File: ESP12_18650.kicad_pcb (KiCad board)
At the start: 2 copper layers, 77.7 x 20.5 mm, 28 parts, among them J1 Conn_02x06_Counter_Clockwise, J10 Conn_01x06_Male, J11 Conn_01x06_Male, J12 Conn_01x06_Male, J13 Conn_01x06_Male, J14 Conn_01x06_Male, J15 Conn_01x06_Male, J16 Conn_01x06_Male, J17 Conn_01x14_Male, J2 Conn_01x14_Male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

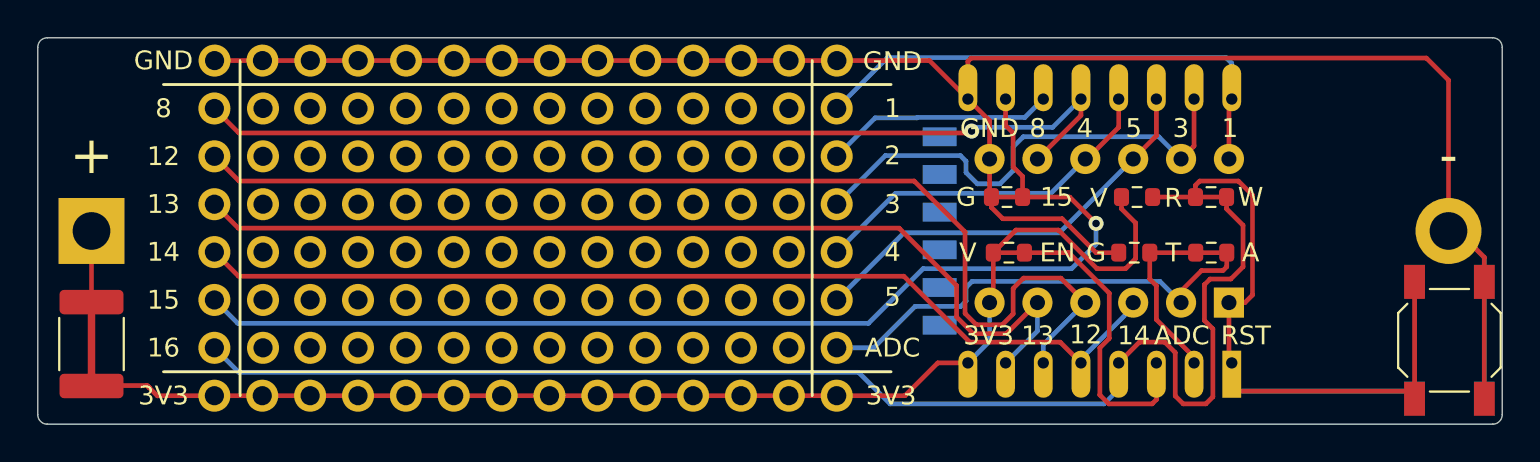
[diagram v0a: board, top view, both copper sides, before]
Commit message: Fix netname and silkscreen for GPIO 0
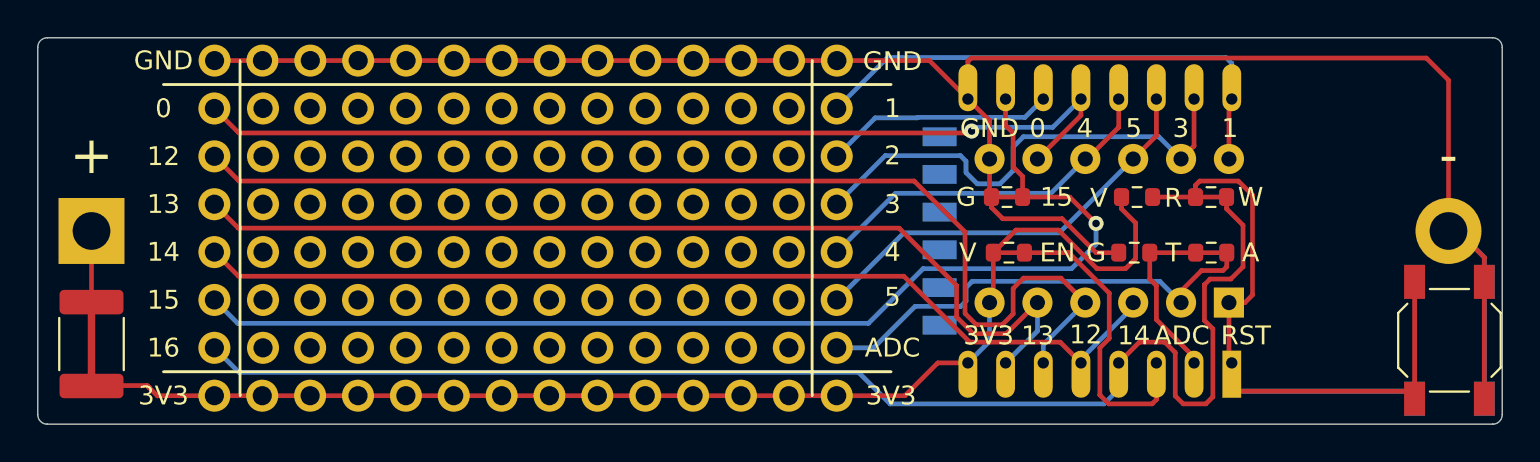
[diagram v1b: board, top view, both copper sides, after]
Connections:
- net /IO8 renamed /IO0
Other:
- board text added: "0"
- board text removed: "8"
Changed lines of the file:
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@@
   (net 14 "unconnected-(U1-Pad14)")
   (net 15 "/IO2")
-  (net 16 "/IO8")
+  (net 16 "/IO0")
   (net 17 "/IO4")
   (net 18 "/IO5")
@@
     )
     (pad "1" thru_hole circle locked (at 0 0 270) (size 1.7 1.7) (drill 1.016) (layers *.Cu *.Mask)
-      (net 16 "/IO8") (pinfunction "Pin_1") (pintype "passive"))
+      (net 16 "/IO0") (pinfunction "Pin_1") (pintype "passive"))
     (pad "2" thru_hole circle locked (at 2.54 0 270) (size 1.7 1.7) (drill 1.016) (layers *.Cu *.Mask)
       (net 7 "/IO12") (pinfunction "Pin_2") (pintype "passive"))
@@
       (net 2 "GND") (pinfunction "Pin_7") (pintype "passive"))
     (pad "8" thru_hole oval (at 7.62 -10.16 90) (size 1.6 1.6) (drill 0.8) (layers *.Cu *.Mask)
-      (net 16 "/IO8") (pinfunction "Pin_8") (pintype "passive"))
+      (net 16 "/IO0") (pinfunction "Pin_8") (pintype "passive"))
     (pad "9" thru_hole oval (at 7.62 -7.62 90) (size 1.6 1.6) (drill 0.8) (layers *.Cu *.Mask)
       (net 17 "/IO4") (pinfunction "Pin_9") (pintype "passive"))
@@
       (net 15 "/IO2") (pinfunction "GPIO2") (pintype "bidirectional"))
     (pad "18" thru_hole oval (at 7 -4.5 90) (size 2.5 1) (drill 0.6 (offset 0.6 0)) (layers *.Cu *.Mask)
-      (net 16 "/IO8") (pinfunction "GPIO0") (pintype "bidirectional"))
+      (net 16 "/IO0") (pinfunction "GPIO0") (pintype "bidirectional"))
     (pad "19" thru_hole oval (at 7 -2.5 90) (size 2.5 1) (drill 0.6 (offset 0.6 0)) (layers *.Cu *.Mask)
       (net 17 "/IO4") (pinfunction "GPIO4") (pintype "bidirectional"))
@@
     (effects (font (size 1 1) (thickness 0.25)) (justify mirror))
   )
-  (gr_text "8" (at 67.818 63.5) (layer "B.SilkS")
+  (gr_text "0" (at 67.818 63.5) (layer "B.SilkS")
     (effects (font (size 1 1) (thickness 0.25)) (justify mirror))
   )
@@
     (effects (font (size 1 1) (thickness 0.25)))
   )
-  (gr_text "8\n" (at 114.2 64.55) (layer "F.SilkS")
+  (gr_text "0" (at 114.2 64.55) (layer "F.SilkS")
     (effects (font (size 1 1) (thickness 0.25)))
   )
@@
     (effects (font (size 1 1) (thickness 0.25)))
   )
-  (gr_text "8" (at 67.818 63.5) (layer "F.SilkS")
-    (effects (font (size 1 1) (thickness 0.25)))
-  )
+  (gr_text "0" (at 67.818 63.5) (layer "F.SilkS")
+    (effects (font (size 1 1) (thickness 0.25)))
+  )

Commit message: Move IO0 to right side, and ADC to left
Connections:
- J16 pad 1: /ADC -> /IO5
- J16 pad 2: /IO5 -> /IO4
- J16 pad 3: /IO4 -> /IO3
- J16 pad 4: /IO3 -> /IO2
- J16 pad 5: /IO2 -> /IO1
- J16 pad 6: /IO1 -> /IO0
- J3 pad 1: /IO0 -> /IO12
- J3 pad 2: /IO12 -> /IO13
- J3 pad 3: /IO13 -> /IO14
- J3 pad 4: /IO14 -> /IO15
- J3 pad 5: /IO15 -> /IO16
- J3 pad 6: /IO16 -> /ADC
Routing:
- net /ADC: track 24.9 -> 59.0 mm
- net /IO0: track 51.4 -> 18.3 mm
- net /EN: track 16.2 -> 10.1 mm
- net /IO15: track 60.2 -> 56.2 mm
- net /IO5: track 22.5 -> 25.5 mm
- net /IO4: track 19.2 -> 21.0 mm
- net /IO3: track 26.0 -> 27.4 mm
- net /IO2: track 12.2 -> 13.4 mm
- net /IO12: track 58.9 -> 60.0 mm
- net /IO1: track 27.3 -> 28.4 mm
- net /IO14: track 52.8 -> 53.8 mm
- net /IO13: track 52.1 -> 53.1 mm
- net /IO16: track 71.9 -> 71.0 mm
- net VCC: track 67.0 -> 67.6 mm

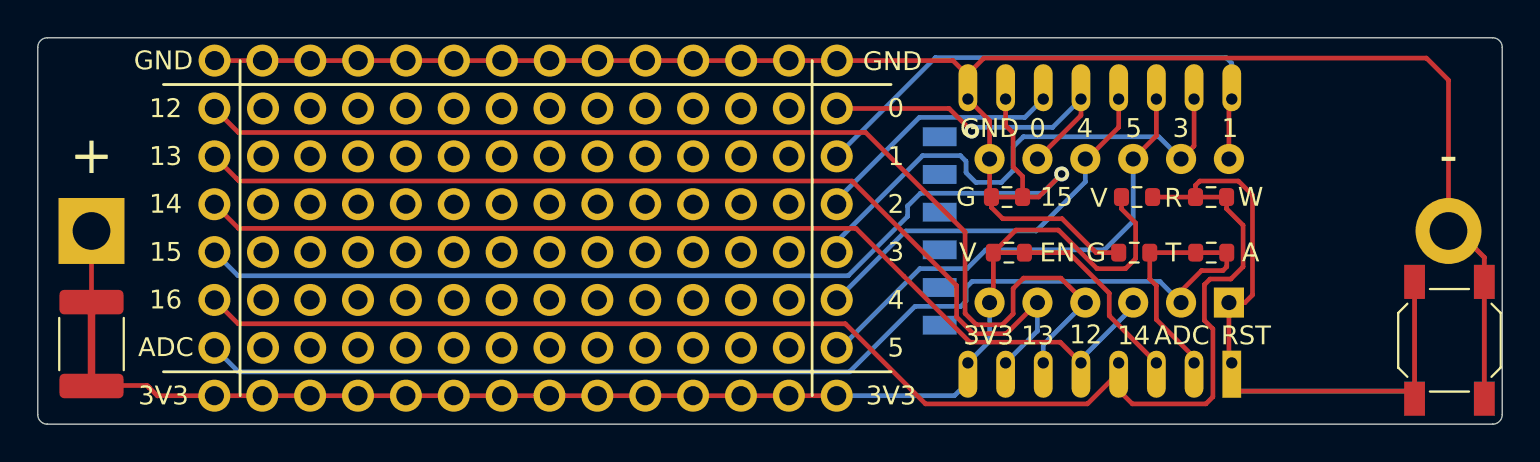
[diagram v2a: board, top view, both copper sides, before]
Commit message: Reorganize connection to eliminate vias
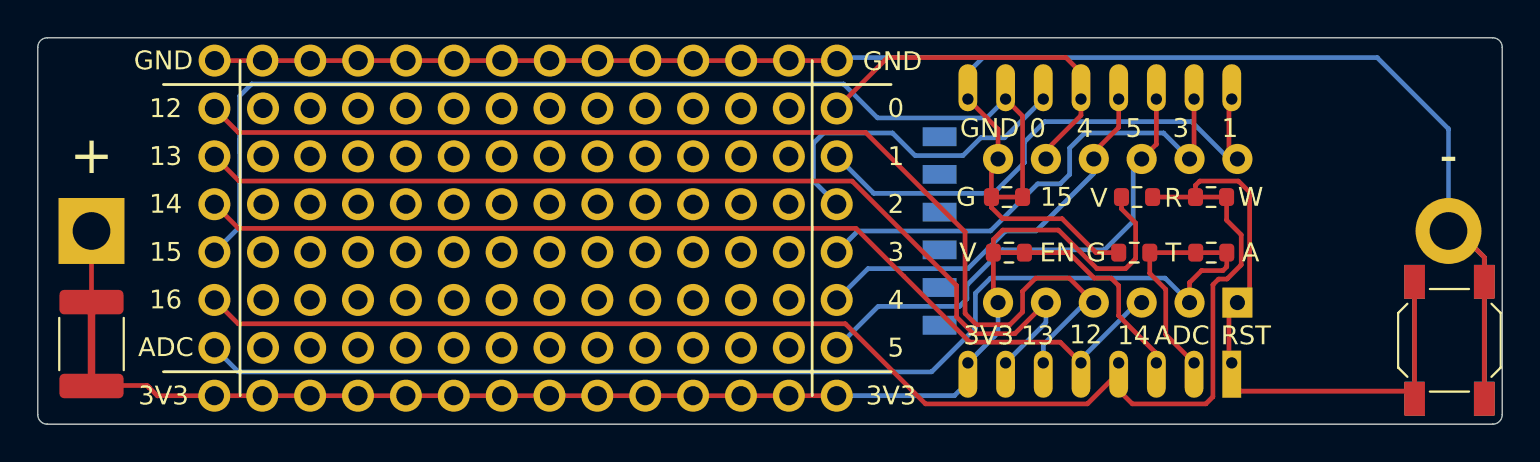
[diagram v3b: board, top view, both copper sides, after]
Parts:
- moved J1 0.45 mm to (124.8, 73.8)
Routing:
- net /IO2: track 13.4 -> 17.9 mm
- net GND: track 112.5 -> 110.9 mm
- net /IO0: track 18.3 -> 19.8 mm, vias 1 -> 0
- net /IO3: track 27.4 -> 26.0 mm
- net /ADC: track 59.0 -> 60.1 mm
- net /IO15: track 56.2 -> 57.2 mm, vias 1 -> 0
- net /IO16: track 71.0 -> 70.2 mm
- net /IO12: track 60.0 -> 60.7 mm
- net /IO13: track 53.1 -> 53.8 mm
- net /RST: track 52.0 -> 51.4 mm
- net VCC: track 67.6 -> 68.2 mm
- net /EN: track 10.1 -> 10.7 mm
